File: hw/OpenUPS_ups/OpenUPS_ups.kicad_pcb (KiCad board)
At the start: 4 copper layers, 96 x 64 mm, 320 parts, among them J1001 USB4105-GF-A, J101 Barrel Jack, J102 XT30PW-M, J103 XT30PW-M, J104 S2B-PH-K_1x02, J105 S2B-PH-K_1x02, J106 Screw Terminal, J107 Screw Terminal, J108 Screw Terminal, J109 JST XH, J110 JST XH, J501 Conn_01x03, J701 0022053031, J702 0022053031, J901 Qwiic, J902 Qwiic, Q1001 2N7002, Q1101 AON7534, Q1102 AON7534, Q1103 BSS84, Q301 AON7534, Q302 AON7534, Q303 AON7534, Q304 AON7534, Q401 2N7002, Q402 AON7534, Q403 AON7534, Q404 AON7534, Q405 AON7534, Q406 AON7423, Q601 AON7534, Q602 AON7534, Q603 AON7534, Q604 AON7534, Q701 2N7002, Q702 2N7002, U1001 MCP6547, U1002 AP22814BW5, U1003 NUP2301MW6T1G, U101 AVR32DB48x-xPT, U102 NUP2301MW6T1G, U103 LM75BTP,147, U1101 BQ76920PW, U1102 π220N31, U201 TPS51397A, U202 INA180A3, U301 NCP81599, U401 NCP431, U402 BD99950, U403 MCP6001R, U404 DZDH0401DW, U405 INA180A1, U601 NCP81599, U701 NUP2301MW6T1G, U702 NUP2301MW6T1G, U801 AP7383-33W5, U901 π220N31

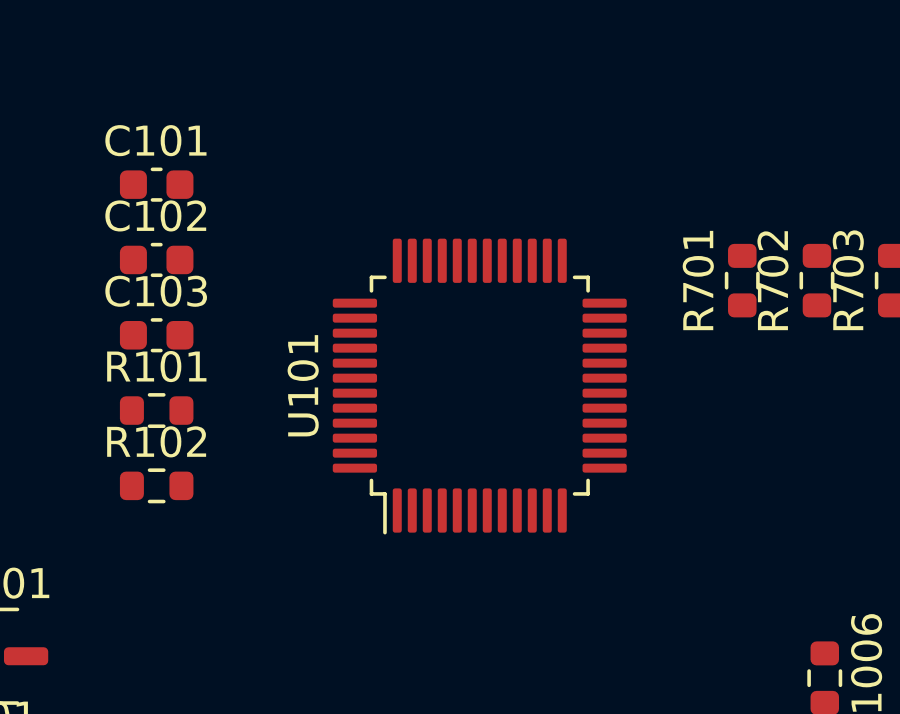
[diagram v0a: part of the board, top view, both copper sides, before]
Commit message: Issue #35 - AVR changed to VQFN 48-pin
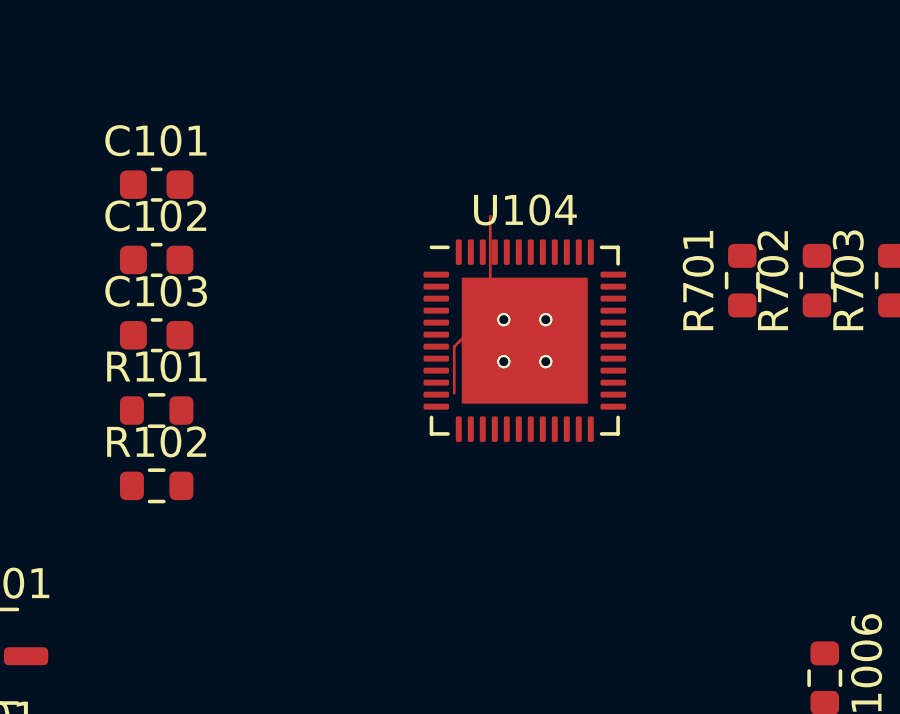
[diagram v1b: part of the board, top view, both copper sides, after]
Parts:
- removed U101: AVR32DB48x-xPT, Package_QFP:TQFP-48_7x7mm_P0.5mm
- added U104: AVR64DB48x-x6LX, Package_DFN_QFN:QFN-48-1EP_6x6mm_P0.4mm_EP4.2x4.2mm, F.Cu at (80.0, 47.0)
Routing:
- net GND: track 91.1 -> 100.9 mm, vias 119 -> 123

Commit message: BMS work
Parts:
- added D1107: BAT54, Package_TO_SOT_SMD:SOT-23, F.Cu at (161.4, 24.6)
- added D1108: SMF5V0A, Diode_SMD:D_SMF, F.Cu at (171.6, 19.6)
- added D1109: SMF5V0A, Diode_SMD:D_SMF, F.Cu at (171.6, 22.9)
- added D1110: SMF5V0A, Diode_SMD:D_SMF, F.Cu at (171.6, 26.3)
- added D1111: SMF5V0A, Diode_SMD:D_SMF, F.Cu at (171.6, 29.6)
- added D1112: BAT54, Package_TO_SOT_SMD:SOT-23, F.Cu at (161.4, 29.1)
- added Q1104: BSS84, Package_TO_SOT_SMD:SOT-23, F.Cu at (161.4, 33.5)
- added Q1105: 2N7002, Package_TO_SOT_SMD:SOT-23, F.Cu at (166.3, 20.1)
- added Q1106: 2N7002, Package_TO_SOT_SMD:SOT-23, F.Cu at (166.3, 24.6)
- added Q1107: BSS84, Package_TO_SOT_SMD:SOT-23, F.Cu at (166.3, 29.1)
- added R1122: 68k, Resistor_SMD:R_0603_1608Metric, F.Cu at (156.9, 21.7)
- added R1123: 100k, Resistor_SMD:R_0603_1608Metric, F.Cu at (156.9, 24.2)
- added R1124: 100k, Resistor_SMD:R_0603_1608Metric, F.Cu at (156.9, 26.7)
- added R1125: 100k, Resistor_SMD:R_0603_1608Metric, F.Cu at (156.9, 29.2)
- added R1126: 10k, Resistor_SMD:R_0603_1608Metric, F.Cu at (156.9, 31.7)
- added R1127: 10k, Resistor_SMD:R_0603_1608Metric, F.Cu at (156.9, 34.2)
- added R1128: NM, Resistor_SMD:R_0603_1608Metric, F.Cu at (156.9, 36.8)
- C1105: value Cf -> 10u 16V; footprint Capacitor_SMD:C_0603_1608Metric -> Capacitor_SMD:C_1206_3216Metric
- C1106, C1108, C1109, C1110: value Cc -> 1u 10V
- C1107: value 0R -> 1u 10V
- D1106: value BAT54J -> BAT54; footprint Diode_SMD:D_SOD-323F -> Package_TO_SOT_SMD:SOT-23
- R1109: value Rf -> 100R
- R1112, R1114, R1115, R1116: value Rc -> 51R
- R1113: value NM -> 51R
- moved D1106 42.6 mm to (161.4, 20.1)
- moved R1109 24.2 mm to (156.9, 19.2)
- moved C1105 23.9 mm to (171.5, 33.0)
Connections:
- C1105 pad 1: -BATT -> Net-(D1112-K)
- C1105 pad 2: Net-(U1101-BAT) -> -BATT
- D1106 pad 1: Net-(D1106-K) -> Net-(D1106-A)
- D1106 pad 2: Net-(D1106-A) -> unconnected-(D1106-NC-Pad2)
- J104 pad 1: /B_TX -> unconnected-(J104-Pin_1-Pad1)
- J104 pad 2: /B_RX -> unconnected-(J104-Pin_2-Pad2)
- R1109 pad 1: Net-(U1101-BAT) -> Net-(D1112-K)
- R1113 pad 2: unconnected-(R1113-Pad2) -> /BMS/VC3
- R1114 pad 2: unconnected-(R1114-Pad2) -> /BMS/VC2
- R1115 pad 2: unconnected-(R1115-Pad2) -> /BMS/VC1
- U104 pad 36: unconnected-(U104-PF2-Pad36) -> /I2C_B_SDA
- U104 pad 37: unconnected-(U104-PF3-Pad37) -> /I2C_B_SCL
- U104 pad 44: /B_TX -> unconnected-(U104-XTALHF1/PA0-Pad44)
- U104 pad 45: /B_RX -> unconnected-(U104-XTALHF2/PA1-Pad45)
- U1101 pad 10: Net-(U1101-BAT) -> Net-(D1112-K)
- U1101 pad 20: unconnected-(U1101-ALERT-Pad20) -> Net-(Q1106-G)

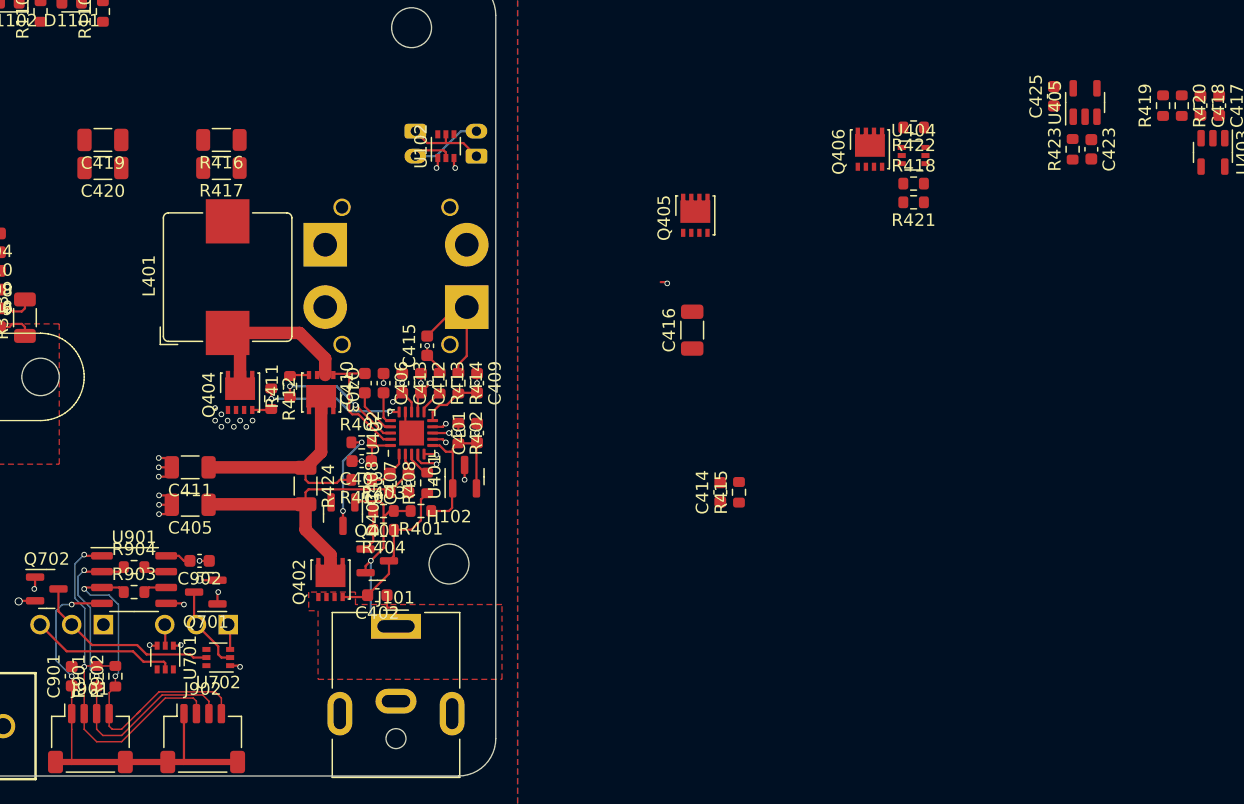
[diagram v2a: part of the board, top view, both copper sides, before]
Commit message: BMS implementation complete (on schematic)
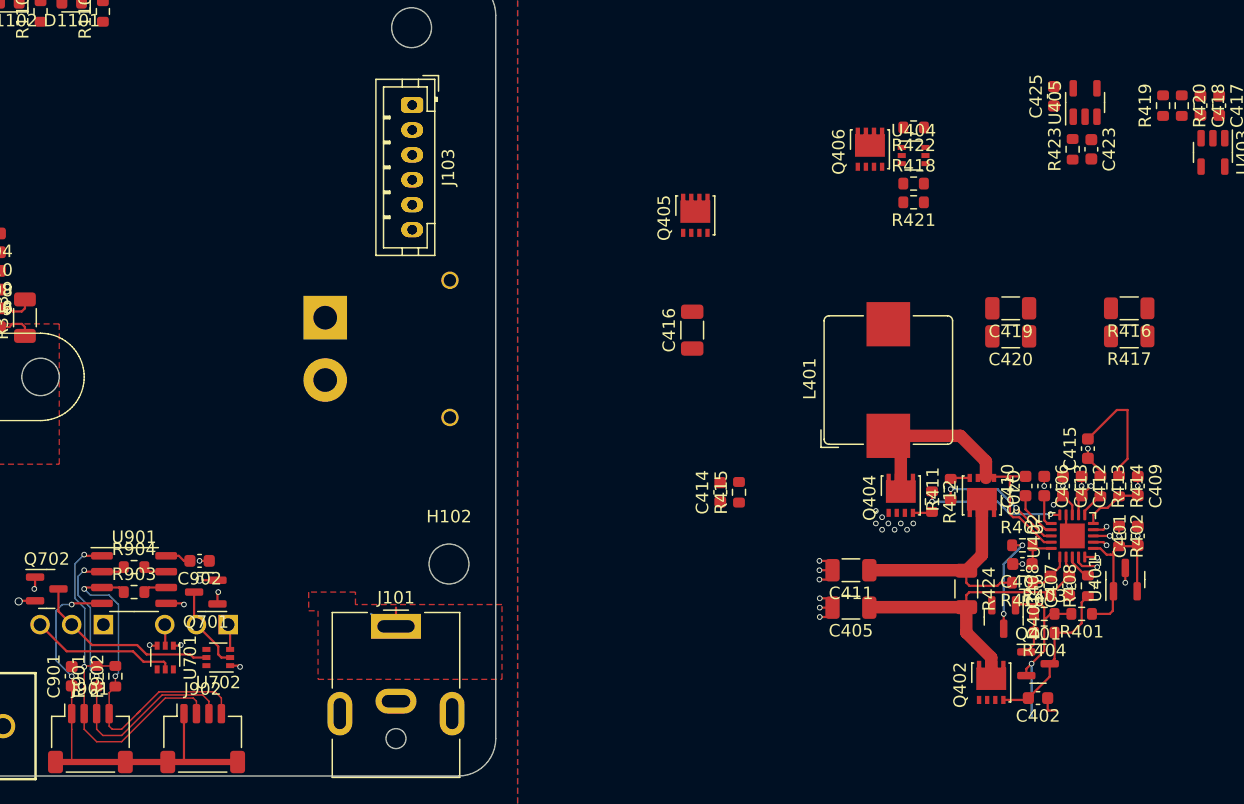
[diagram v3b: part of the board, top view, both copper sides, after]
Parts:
- removed J104: S2B-PH-K_1x02, Connector_JST:JST_PH_S2B-PH-K_1x02_P2.00mm_Horizontal
- removed U102: NUP2301MW6T1G, Package_TO_SOT_SMD:SOT-363_SC-70-6
- J103: value XT30PW-M -> B6B-PH-K_1x06; footprint Connector_AMASS:AMASS_XT30PW-M_1x02_P2.50mm_Horizontal -> Connector_JST:JST_PH_B6B-PH-K_1x06_P2.00mm_Vertical; moved to F.Cu
- J105: value S2B-PH-K_1x02 -> S6B-PH-K_1x06; footprint Connector_JST:JST_PH_S2B-PH-K_1x02_P2.00mm_Horizontal -> Connector_JST:JST_PH_S6B-PH-K_1x06_P2.00mm_Horizontal
- moved C419 74.0 mm to (220.3, 96.5)
- moved C420 74.0 mm to (220.3, 98.8)
- moved R416 74.0 mm to (229.8, 96.5)
- moved R417 74.0 mm to (229.8, 98.8)
- moved C401 53.6 mm to (230.5, 114.8)
- moved C402 53.6 mm to (222.5, 127.8)
- moved C403 53.6 mm to (221.2, 117.0)
- moved C405 53.6 mm to (207.5, 120.5)
- moved C406 53.6 mm to (223.0, 110.8)
- moved C407 53.6 mm to (225.0, 118.8)
- moved C408 53.6 mm to (223.5, 118.8)
- moved C409 53.6 mm to (230.5, 110.8)
- moved C410 53.6 mm to (221.5, 110.8)
- moved C411 53.6 mm to (207.5, 117.5)
- moved C412 53.6 mm to (226.0, 110.8)
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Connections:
- net /BMS/ALERT renamed /BMS_ALERT
- net /BMS/WAKEUP renamed /BMS_WKUP
- J102 pad 2: GND -> -BATT
- J103 pad 1: +BATT -> /I2C_B_SCL
- J103 pad 2: GND -> /I2C_B_SDA
- J105 pad 1: /B_TX -> /I2C_B_SCL
- J105 pad 2: /B_RX -> /I2C_B_SDA
- R1110 pad 1: /BMS/SCL -> /I2C_B_SCL
- R1111 pad 1: /BMS/SDA -> /I2C_B_SDA
- R1113 pad 2: /BMS/VC3 -> /VC3
- R1114 pad 2: /BMS/VC2 -> /VC2
- R1115 pad 2: /BMS/VC1 -> /VC1
- R1128 pad 1: /BMS/VC2 -> /VC2
- R1128 pad 2: /BMS/VC3 -> /VC3
- U1102 pad 2: /BMS/SDA -> /I2C_B_SDA
- U1102 pad 3: /BMS/SCL -> /I2C_B_SCL
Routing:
- net /B_RX: track 8.89 -> 0.00 mm
- net /B_TX: track 6.43 -> 0.00 mm
- net GND: track 100.9 -> 100.0 mm, vias 123 -> 122
- net +3.3VA: track 8.07 -> 7.23 mm, vias 5 -> 4
- net Net-(Q405-G): track 3.16 -> 2.59 mm, vias 2 -> 1

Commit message: PCB multitasking
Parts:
- removed R1128, R903, R904: NM, Resistor_SMD:R_0603_1608Metric
- moved U103 108.1 mm to (218.0, 44.0)
- moved R1109 70.1 mm to (159.5, 89.2), turned to -90 degrees
- moved D1109 62.9 mm to (167.8, 85.8), turned to 90 degrees
- moved D1108 61.6 mm to (167.8, 81.0), turned to 90 degrees
- moved D1111 61.0 mm to (167.8, 90.5), turned to 90 degrees
- moved D1112 60.3 mm to (163.1, 89.3), turned to 180 degrees
- moved C1105 57.8 mm to (156.2, 88.8), turned to 180 degrees
- moved D1110 51.5 mm to (166.0, 77.5), turned to 180 degrees
- moved Q1103 42.8 mm to (170.0, 20.8)
- moved R1112 41.3 mm to (165.8, 90.8), turned to -90 degrees
- moved R1113 39.8 mm to (176.0, 90.2), turned to 180 degrees
- moved C1103 38.3 mm to (155.5, 85.2)
- moved R1108 38.3 mm to (160.5, 24.2)
- moved C1109 37.8 mm to (165.0, 79.5), turned to 180 degrees
- moved C1104 37.3 mm to (155.5, 86.8)
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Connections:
- J103 pad 1: /I2C_B_SCL -> VBMS
- J103 pad 2: /I2C_B_SDA -> /BMS/BMS_SDA
- J103 pad 3: VBMS -> /BMS/BMS_SCL
- J103 pad 4: /VC3 -> /VC1
- J103 pad 6: /VC1 -> /VC3
- J105 pad 1: /I2C_B_SCL -> VBMS
- J105 pad 2: /I2C_B_SDA -> /BMS/BMS_SDA
- J105 pad 3: VBMS -> /BMS/BMS_SCL
- J105 pad 4: /VC3 -> /VC1
- J105 pad 6: /VC1 -> /VC3
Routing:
- net /Ext. I2C Interface/XI2C_GND: track 35.0 -> 2.39 mm, vias 2 -> 0
- net /F_Tach0: track 1.71 -> 13.5 mm, vias 0 -> 1
- net /Ext. I2C Interface/XI2C_SDA: track 28.7 -> 21.7 mm, vias 2 -> 3
- net /Ext. I2C Interface/XI2C_SCL: track 28.9 -> 22.1 mm, vias 2 -> 3
- net /F_PWM1: track 0.98 -> 7.31 mm
- net /F_PWM0: track 0.98 -> 7.31 mm, vias 1 -> 0
- net Net-(J702-Pin_2): track 15.2 -> 21.4 mm
- net /Ext. I2C Interface/XI2C_VCC: track 31.6 -> 26.3 mm
- net /F_Tach1: track 11.8 -> 6.82 mm
- net /I2C_E_SCL: track 1.90 -> 5.19 mm
- net /I2C_E_SDA: track 1.90 -> 4.97 mm
- net +12V: track 24.8 -> 26.5 mm
- net Net-(J701-Pin_2): track 6.86 -> 8.44 mm
- net +3.3VA: track 7.23 -> 8.24 mm, vias 4 -> 5
- net GND: track 100.0 -> 99.5 mm, vias 122 -> 121
- added copper zone on F.Cu, net /Ext. I2C Interface/XI2C_GND
